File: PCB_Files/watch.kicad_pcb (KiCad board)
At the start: 2 copper layers, 60 x 60 mm, 117 parts, among them J1 Conn_01x02_Pin, J3 Conn_01x02_Pin, P1 USB_C_Plug_USB2.0, Q1 BC847, Q2 BC847, Q4 BSS138, Q5 BSS138, Q8 BC847, SW1 SW_Push, SW2 SW_Push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

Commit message: Completed layout
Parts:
- removed R26, R27: 33, Resistor_SMD:R_0603_1608Metric
- added J2: Conn_01x14_MountingPin, footprints:HRS_FH34SRJ-14S-0.5SH_50_, F.Cu at (83.1, 86.4)
- added R13: 10k, Resistor_SMD:R_0603_1608Metric, F.Cu at (99.6, 70.7)
- added R7: 10k, Resistor_SMD:R_0603_1608Metric, F.Cu at (100.1, 73.9)
- D9: footprint footprints:SOD-123FL -> Diode_SMD:D_SOD-123
- FB1: value FerriteBead -> 2.66
- moved TP6 95.1 mm to (78.5, 96.8)
- moved TP3 92.9 mm to (89.3, 102.5)
- moved TP4 91.5 mm to (77.0, 93.3)
- moved TP1 75.0 mm to (102.8, 91.7)
- moved TP5 73.9 mm to (90.5, 75.7)
- moved TP7 71.5 mm to (114.4, 89.1), turned to 180 degrees
- moved TP2 70.7 mm to (103.4, 90.2)
- moved TP8 67.4 mm to (114.4, 87.4), turned to 180 degrees
- moved Q8 31.1 mm to (80.5, 76.7)
- moved R37 30.3 mm to (84.9, 75.4), turned to 0 degrees
- moved R36 25.3 mm to (81.9, 79.2), turned to -90 degrees
- moved C32 14.9 mm to (77.9, 77.7), turned to 90 degrees
- moved AE1 13.8 mm to (96.5, 62.9), turned to 10 degrees
- moved J1 10.8 mm to (84.0, 101.1), turned to 50 degrees
- moved R22 9.47 mm to (99.3, 72.4), turned to 180 degrees
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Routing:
- net /SDA: track 0.00 -> 62.2 mm, vias 0 -> 5
- net /SCL_i2c: track 0.00 -> 59.7 mm, vias 0 -> 5
- net /CTP_INT: track 0.00 -> 45.6 mm, vias 0 -> 2
- net /RS: track 0.00 -> 41.3 mm, vias 0 -> 2
- net GND: track 70.3 -> 111.3 mm, vias 27 -> 50
- net /EN: track 26.9 -> 65.0 mm, vias 2 -> 5
- net /MISO: track 0.00 -> 35.0 mm, vias 0 -> 3
- net /BL_PWM: track 0.00 -> 27.3 mm, vias 0 -> 2
- net /MOSI: track 0.00 -> 26.5 mm, vias 0 -> 3
- net /CS_DISPLAY: track 0.00 -> 25.2 mm, vias 0 -> 2
- net /INTR1_IMU: track 0.00 -> 25.1 mm, vias 0 -> 2
- net /VCC_RF: track 0.00 -> 15.2 mm
- net /SCL: track 11.2 -> 26.1 mm, vias 2 -> 3
- net /BTN2: track 0.00 -> 10.7 mm, vias 0 -> 2
- net /BTN1: track 0.00 -> 10.5 mm, vias 0 -> 2
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- removed copper zone on F.Cu, net GND
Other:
- board size 60 x 60 mm -> 52 x 52 mm

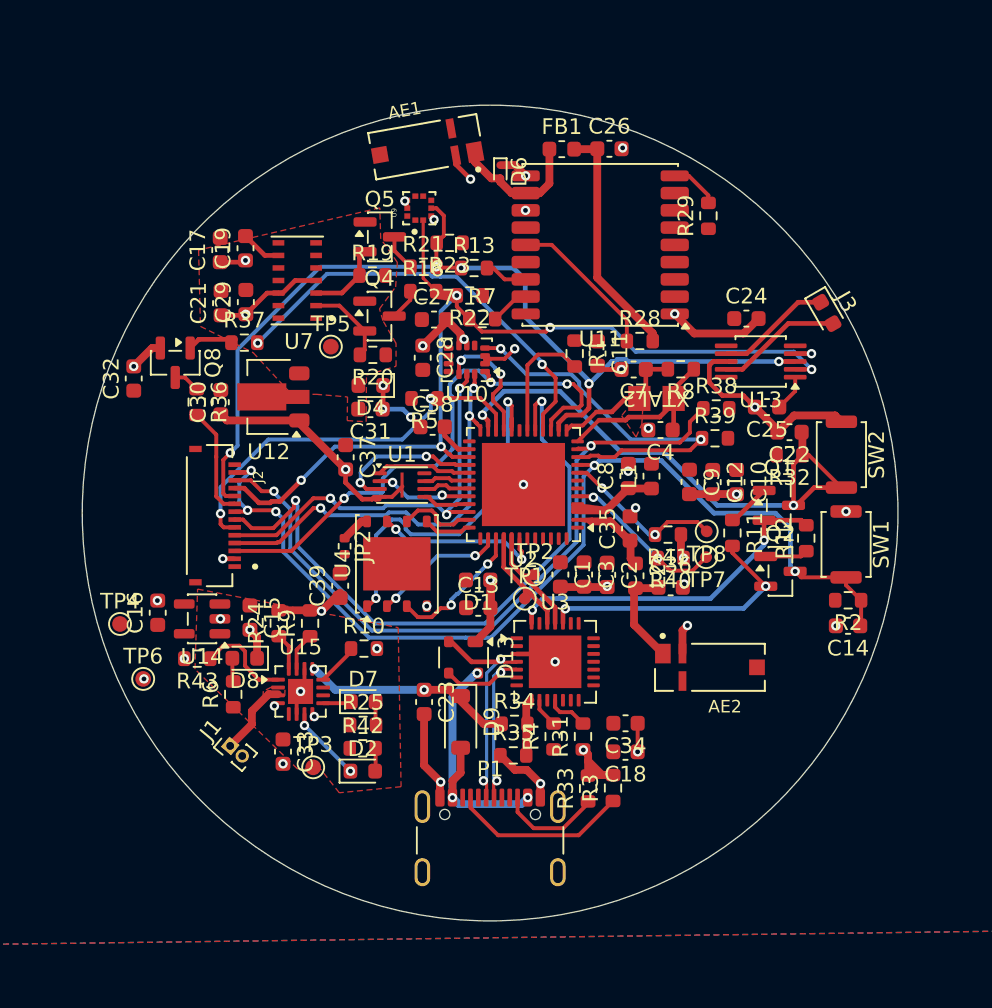
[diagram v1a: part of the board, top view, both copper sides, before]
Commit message: Did impedance matching of antennas
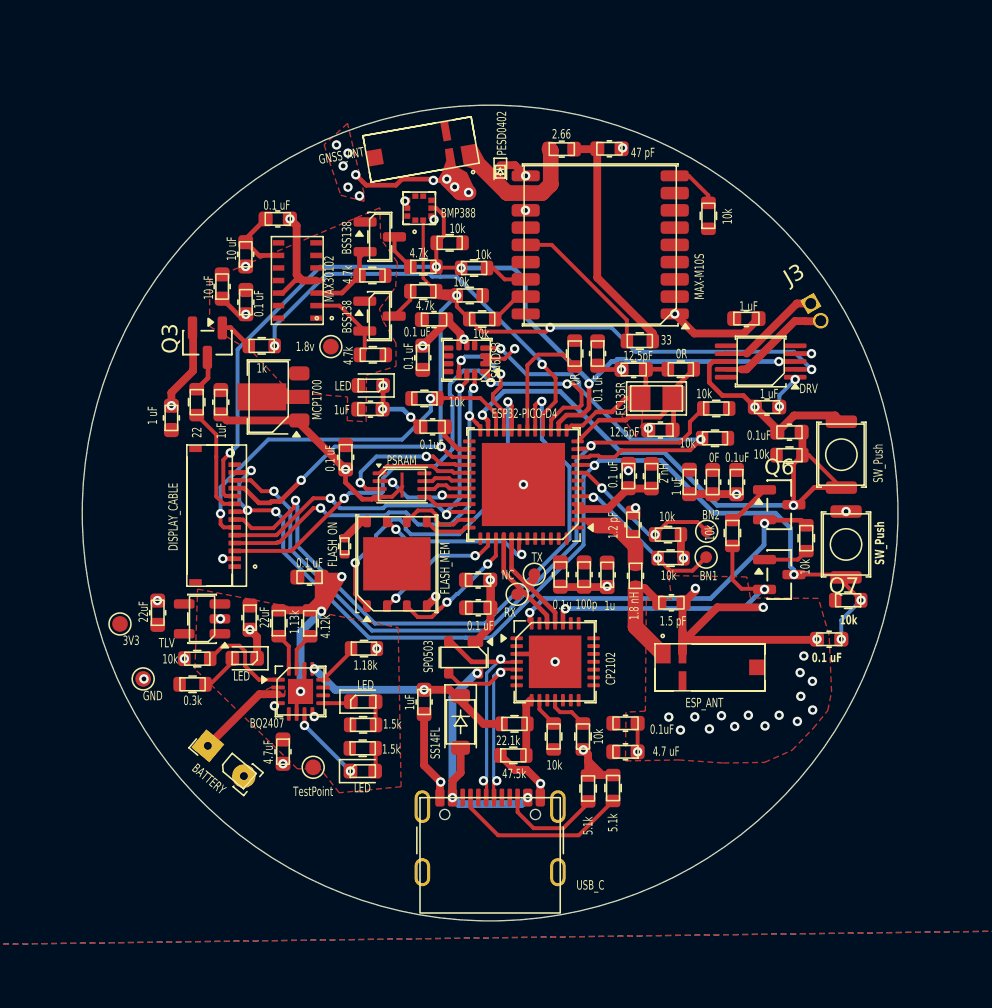
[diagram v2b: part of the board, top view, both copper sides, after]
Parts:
- removed Q1, Q2, Q8: BC847, Package_TO_SOT_SMD:SOT-23
- added Q3: SS8050, Package_TO_SOT_SMD:SOT-23, F.Cu at (82.6, 75.4)
- added Q6: SS8050, Package_TO_SOT_SMD:SOT-23, F.Cu at (119.0, 85.7)
- added Q7: SS8050, Package_TO_SOT_SMD:SOT-23, F.Cu at (119.0, 90.2)
- AE1: value Antenna_Shield -> GNSS_ANT
- AE2: value Antenna_Shield -> ESP_ANT
- C1: value 0.1 uF -> 0.1u
- C10, C22, C34: value 0.1 uF -> 0.1uF
- C12: value 0 F -> 0F
- C2: value 1 uF -> 1u
- C3: value 100 pF -> 100p
- D13: value SP0503BAHT -> SP0503
- D6: value PESD0402-0402T -> PESD0402
- J1: value Conn_01x02_Pin -> BATTERY
- J2: value Conn_01x14_MountingPin -> DISPLAY_CABLE
- J3: value Conn_01x02_Pin -> MOTOR; footprint Diode_SMD:D_0603_1608Metric -> Connector_PinSocket_1.27mm:PinSocket_1x02_P1.27mm_Vertical
- JP2: value SolderJumper_2_Open -> FLASH_ON
- P1: value USB_C_Plug_USB2.0 -> USB_C
- TP1: value TestPoint -> RX
- TP2: value TestPoint -> TX
- TP4: value TestPoint -> 3V3
- TP5: value TestPoint -> 1.8v
- TP6: value TestPoint -> GND
- TP7: value TestPoint -> BN1
- TP8: value TestPoint -> BN2
- U1: value APS6404L-3SQRx-ZR -> PSRAM
- U12: value MCP1700x-120xxMB -> MCP1700
- U13: value DRV2605LDGS -> DRV
- U14: value TLV75533PDBV -> TLV
- U15: value BQ24074RGT -> BQ2407
- U3: value CP2102N-Axx-xQFN28 -> CP2102
- U4: value W25Q128JVP -> FLASH_MEM
- U7: value MAX30105EFD_T -> MAX30102
- XTAL2: value FC-135R 32.7680KA-A3 -> FC135R
- moved C17 4.17 mm to (87.1, 67.5), turned to 180 degrees
- moved C32 3.47 mm to (80.3, 80.2)
- moved R6 2.67 mm to (81.6, 97.2), turned to 0 degrees
- moved C39 2.03 mm to (89.1, 90.4), turned to 180 degrees
- moved C14 1.48 mm to (122.2, 94.3)
- moved J1 1.28 mm to (84.1, 102.4)
- moved J3 1.18 mm to (121.0, 72.9), turned to 30 degrees
- moved R37 1.13 mm to (86.0, 75.6)
- moved C21 1.06 mm to (83.5, 71.8)
- moved C36 0.98 mm to (112.2, 92.0)
- moved TP1 0.56 mm to (102.3, 91.5)
- moved C19 0.39 mm to (85.0, 69.8)
- moved AE1 0.37 mm to (96.2, 63.1)
- moved C35 0.31 mm to (109.7, 87.0)
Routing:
- net GND: track 111.3 -> 154.4 mm, vias 50 -> 76
- net /3V3: track 2.61 -> 4.46 mm
- net /EN: track 65.0 -> 66.5 mm, vias 5 -> 7
- net Net-(Q3-B): track 3.32 -> 2.13 mm
- net /BAT+: track 4.90 -> 5.84 mm
- net /RTS: track 17.8 -> 18.7 mm
- net /U0RXD: track 7.50 -> 6.80 mm
- net /U0TXD: track 8.27 -> 7.58 mm
- net Net-(Q3-C): track 1.68 -> 2.34 mm
- net /Motor_OUT+: track 7.37 -> 6.72 mm
- net /Motor_OUT-: track 8.02 -> 7.39 mm
- net Net-(D8-A): track 1.50 -> 2.13 mm
- net /CS_ROM: track 23.2 -> 23.8 mm
- net Net-(AE1-A): track 8.77 -> 8.25 mm
- net Net-(U13-REG): track 2.33 -> 2.16 mm, vias 0 -> 2
- added copper zone on F.Cu, net GND

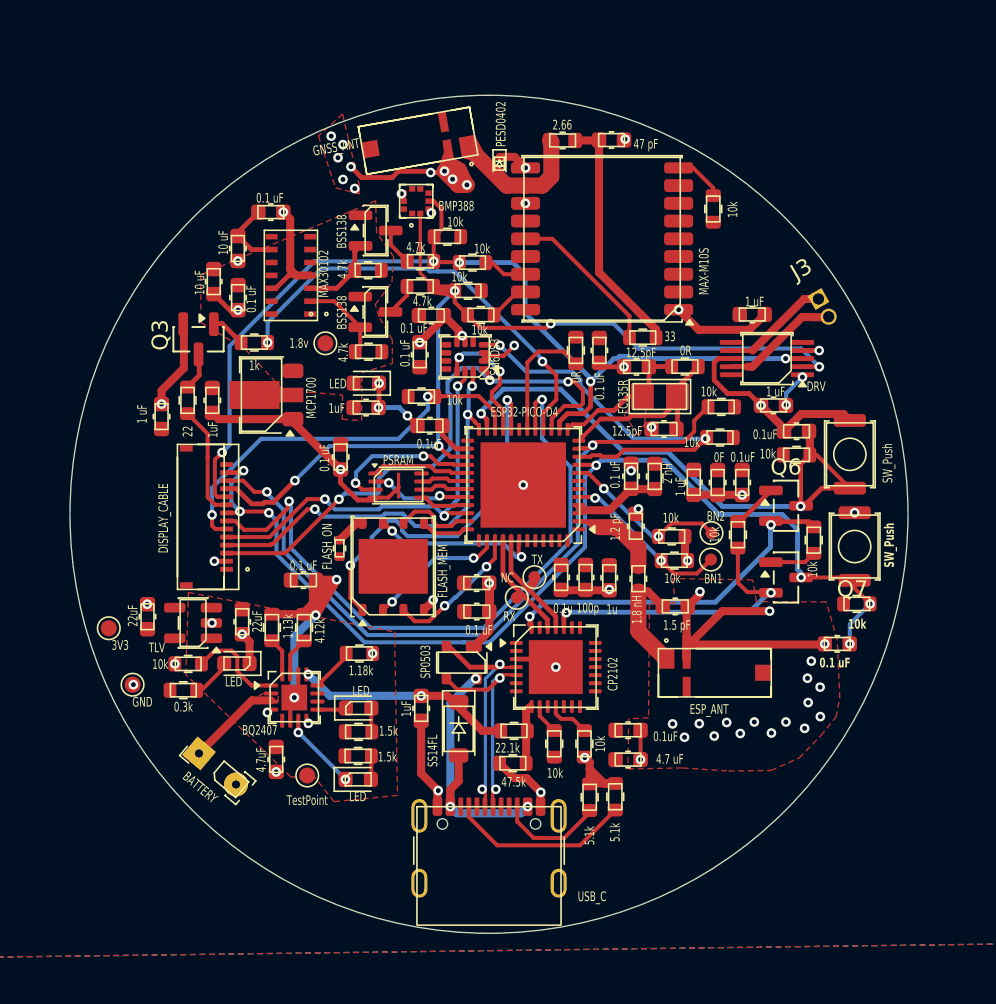
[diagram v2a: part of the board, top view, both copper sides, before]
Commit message: Improving Antenna routing
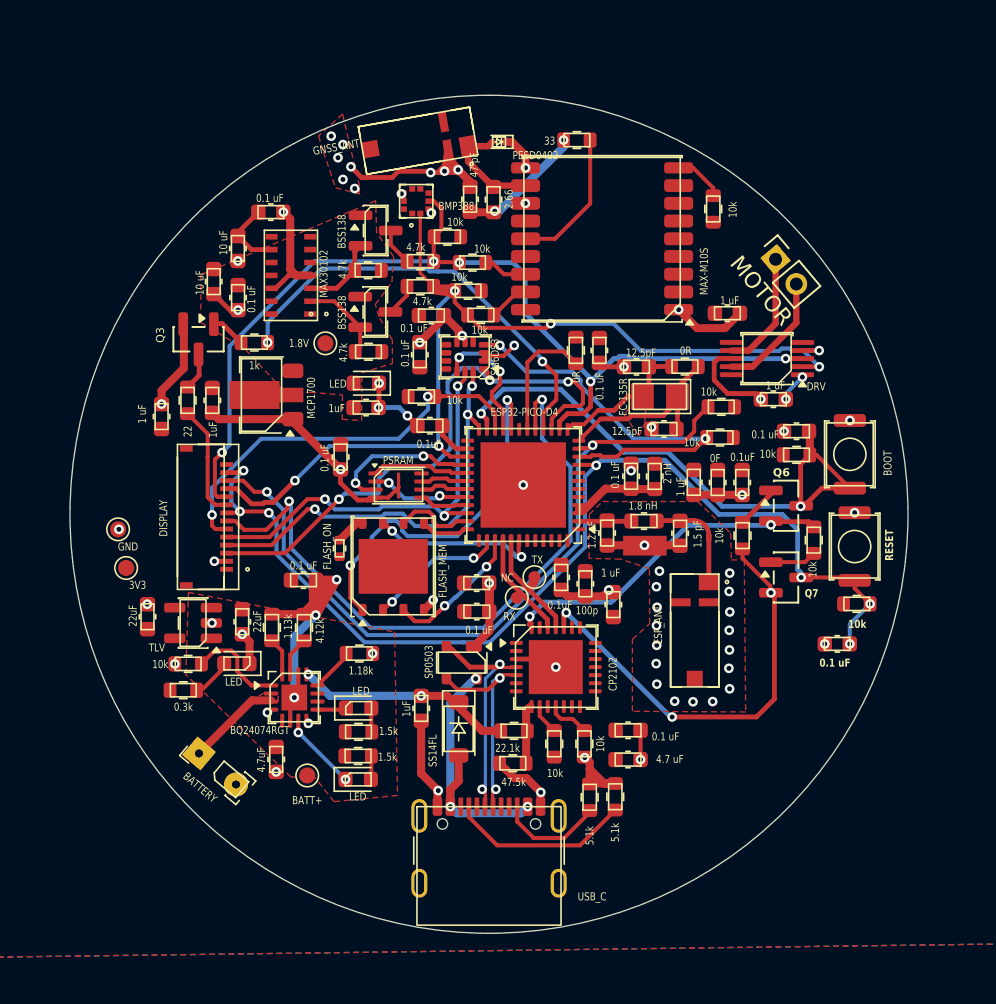
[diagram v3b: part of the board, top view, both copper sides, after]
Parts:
- removed R40, R41: 10k, Resistor_SMD:R_0603_1608Metric
- removed TP7: BN1, TestPoint:TestPoint_Pad_D1.0mm
- removed TP8: BN2, TestPoint:TestPoint_Pad_D1.0mm
- C1: value 0.1u -> 0.1uF
- C2: value 1u -> 1 uF
- C22, C34: value 0.1uF -> 0.1 uF
- J2: value DISPLAY_CABLE -> DISPLAY
- MOTOR: renamed from J3; value MOTOR -> Conn_01x02_Pin; footprint Connector_PinSocket_1.27mm:PinSocket_1x02_P1.27mm_Vertical -> Connector_PinSocket_2.00mm:PinSocket_1x02_P2.00mm_Vertical
- SW1: value SW_Push -> RESET
- SW2: value SW_Push -> BOOT
- TP3: value TestPoint -> BATT+
- TP5: value 1.8v -> 1.8V
- U15: value BQ2407 -> BQ24074RGT
- XTAL2: value FC135R -> FC-135R
- moved R28 12.9 mm to (106.1, 63.1), turned to 180 degrees
- moved TP6 9.68 mm to (77.6, 87.2)
- moved C26 9.52 mm to (99.4, 66.7), turned to 90 degrees
- moved FB1 5.64 mm to (100.9, 66.7), turned to -90 degrees
- moved C36 4.55 mm to (112.5, 87.4), turned to -90 degrees
- moved TP4 3.89 mm to (78.1, 89.6)
- moved MOTOR 3.62 mm to (118.4, 70.5), turned to 40 degrees
- moved L2 3.60 mm to (110.2, 86.7), turned to 0 degrees
- moved AE2 2.90 mm to (113.4, 93.5), turned to 90 degrees
- moved C35 1.83 mm to (107.9, 87.4), turned to -90 degrees
- moved C2 1.68 mm to (108.3, 91.9), turned to 90 degrees
- moved C24 1.55 mm to (115.4, 73.8)
- moved D6 1.35 mm to (101.2, 63.2), turned to 180 degrees
- moved C3 0.39 mm to (106.6, 90.6)
- moved C25 0.39 mm to (118.2, 79.1)
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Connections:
- U2 pad 5: /BTN1 -> unconnected-(U2-SENSOR_VP-Pad5)
- U2 pad 8: /BTN2 -> unconnected-(U2-SENSOR_VN-Pad8)
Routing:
- net GND: track 154.4 -> 128.7 mm, vias 76 -> 75
- net /BTN2: track 10.7 -> 0.00 mm, vias 2 -> 0
- net /BTN1: track 10.5 -> 0.00 mm, vias 2 -> 0
- net /RTS: track 18.7 -> 27.1 mm, vias 2 -> 3
- net /VCC_RF: track 15.2 -> 7.93 mm, vias 0 -> 2
- net Net-(AE1-A): track 8.25 -> 6.80 mm
- net Net-(AE2-A): track 6.78 -> 5.64 mm
- net /LNA_IN: track 4.18 -> 3.12 mm
- net Net-(U11-VCC_RF): track 9.77 -> 8.86 mm
- net /DTR: track 21.9 -> 21.1 mm
- net /Motor_OUT+: track 6.72 -> 7.42 mm

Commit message: Fixed some routing
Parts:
- AE1: value GNSS_ANT -> Antenna_Shield
- AE2: value ESP_ANT -> Antenna_Shield
- C1, C10: value 0.1uF -> 0.1 uF
- C12: value 0F -> 0 F
- C26: footprint Capacitor_SMD:C_0603_1608Metric -> Capacitor_SMD:C_0402_1005Metric
- C3: value 100p -> 100 pF
- D13: value SP0503 -> SP0503BAHT
- D6: value PESD0402 -> PESD0402-0402T
- FB1: footprint Inductor_SMD:L_0603_1608Metric -> Inductor_SMD:L_0402_1005Metric
- J1: value BATTERY -> Conn_01x02_Pin
- J2: value DISPLAY -> Conn_01x14_MountingPin
- J3: renamed from MOTOR; footprint Connector_PinSocket_2.00mm:PinSocket_1x02_P2.00mm_Vertical -> Connector_PinSocket_1.27mm:PinSocket_1x02_P1.27mm_Vertical
- JP2: value FLASH_ON -> SolderJumper_2_Open
- P1: value USB_C -> USB_C_Plug_USB2.0
- R28: footprint Resistor_SMD:R_0603_1608Metric -> Resistor_SMD:R_0402_1005Metric
- SW1: value RESET -> SW_Push
- SW2: value BOOT -> SW_Push
- TP1: value RX -> TestPoint
- TP2: value TX -> TestPoint
- TP3: value BATT+ -> TestPoint
- TP4: value 3V3 -> TestPoint
- TP5: value 1.8V -> TestPoint
- TP6: value GND -> TestPoint
- U1: value PSRAM -> APS6404L-3SQRx-ZR
- U12: value MCP1700 -> MCP1700x-120xxMB
- U13: value DRV -> DRV2605LDGS
- U14: value TLV -> TLV75533PDBV
- U3: value CP2102 -> CP2102N-Axx-xQFN28
- U4: value FLASH_MEM -> W25Q128JVP
- U7: value MAX30102 -> MAX30105EFD_T
- XTAL2: value FC-135R -> FC-135R 32.7680KA-A3
- moved R28 8.23 mm to (100.6, 69.2)
- moved D6 3.43 mm to (100.0, 66.4), turned to 90 degrees
- moved C1 3.29 mm to (108.3, 90.7), turned to 90 degrees
- moved R12 2.12 mm to (118.7, 88.3), turned to 0 degrees
- moved C2 1.91 mm to (109.8, 90.7)
- moved C26 1.55 mm to (100.5, 67.8), turned to 180 degrees
- moved AE1 0.87 mm to (95.4, 63.5), turned to 15 degrees
- moved U9 0.72 mm to (96.8, 67.1)
- moved Q7 0.72 mm to (119.3, 90.9)
- moved TP2 0.59 mm to (103.1, 89.7)
- moved J3 0.51 mm to (118.4, 71.0)
- moved C32 0.51 mm to (79.8, 80.2)
- moved FB1 0.39 mm to (101.0, 66.4)
- moved C3 0.26 mm to (106.8, 90.7), turned to 90 degrees
- moved R23 0.06 mm to (98.0, 69.1)
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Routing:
- net GND: track 128.7 -> 98.5 mm, vias 75 -> 131
- net /DTR: track 21.1 -> 32.3 mm
- net Net-(U11-VCC_RF): track 8.86 -> 1.81 mm
- net /VCC_RF: track 7.93 -> 2.69 mm, vias 2 -> 0
- net /3V3: track 4.46 -> 0.21 mm
- net Net-(AE1-A): track 6.80 -> 5.58 mm
- net /SDA: track 62.2 -> 63.3 mm, vias 5 -> 6
- net /LNA_IN: track 3.12 -> 2.05 mm
- net Net-(Q7-B): track 2.88 -> 1.86 mm
- net /EN: track 66.5 -> 67.3 mm
- net /BL_PWM: track 27.0 -> 26.4 mm
- net /Motor_OUT+: track 7.42 -> 6.91 mm
- net /SCL_i2c: track 59.8 -> 60.2 mm, vias 5 -> 6
- removed copper zone on F.Cu, net /32K_P
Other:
- board text added: "0.1 uF"
- board text added: "0.1uF"
- board text added: "0.3k"
- board text added: "0F"
- board text added: "0R"
- board text added: "1 uF"
- board text added: "1.13k"
- board text added: "1.18k"
- board text added: "1.2 pF"
- board text added: "1.5 pF"
- board text added: "1.5k"
- board text added: "1.8 nH"
- board text added: "1.8V"
- board text added: "10 uF"
- board text added: "100p"
- board text added: "10k"
- board text added: "12.5pF"
- board text added: "1k"
- board text added: "1u"
- board text added: "1uF"
- board text added: "2 nH"
- board text added: "2.66"
- board text added: "22"
- board text added: "22.1k"
- board text added: "22uF"
- board text added: "33"
- board text added: "3V3"
- board text added: "4.12k"
- board text added: "4.7 uF"
- board text added: "4.7k"
- board text added: "4.7uF"
- board text added: "47.5k"
- board text added: "47p"
- board text added: "5.1k"
- board text added: "BATT+"
- board text added: "BATTERY"
- board text added: "BMP388"
- board text added: "BOOT"
- board text added: "BQ24074RGT"
- board text added: "BSS138"
- board text added: "CP2102"
- board text added: "DISPLAY"
- board text added: "DRV"
- board text added: "ESP32-PICO-D4"
- board text added: "ESP_ANT"
- board text added: "FC-135R"
- board text added: "FLASH_MEM"
- board text added: "FLASH_ON"
- board text added: "GND"
- board text added: "GNSS_ANT"
- board text added: "LED"
- board text added: "LSM6DS3"
- board text added: "MAX-M10S"
- board text added: "MAX30102"
- board text added: "MCP1700"
- board text added: "MOTOR"
- board text added: "NC"
- board text added: "PESD0402"
- board text added: "PSRAM"
- board text added: "Q3"
- board text added: "Q6"
- board text added: "Q7"
- board text added: "RESET"
- board text added: "RX"
- board text added: "SP0503"
- board text added: "SS14FL"
- board text added: "TLV"
- board text added: "TX"
- board text added: "USB_C"
